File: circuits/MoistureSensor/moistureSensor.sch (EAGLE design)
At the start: 2 parts, among them Q1 BSS84

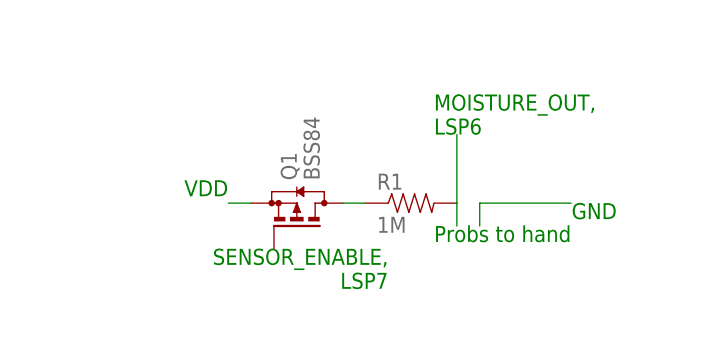
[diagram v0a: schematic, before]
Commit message: Added Moisture Sensor layout
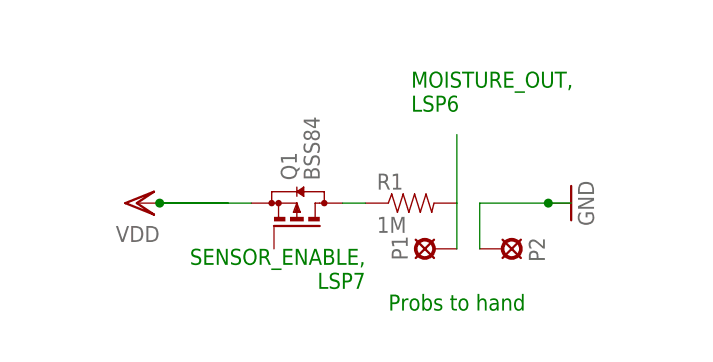
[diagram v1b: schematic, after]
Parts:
- added P1, P2: MCS10B, solpad:MCS10B
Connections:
- net N$2 renamed VDD
- new net GND: P2.MP
- net N$3: now also P1.MP
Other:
- note removed: "GND"
- note removed: "VDD"
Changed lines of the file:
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@@
 <part name="R1" library="SparkFun-Resistors" deviceset="1MOHM-1/10W-1%(0603)" device="" value="1M"/>
 <part name="Q1" library="transistor-small-signal" deviceset="BSS84" device=""/>
+<part name="GND1" library="supply1" deviceset="GND" device=""/>
+<part name="VDD1" library="supply1" deviceset="VDD" device=""/>
+<part name="P1" library="solpad" deviceset="MCS10B" device=""/>
+<part name="P2" library="solpad" deviceset="MCS10B" device=""/>
 </parts>
 <sheets>
 <sheet>
 <plain>
-<text x="12.7" y="66.04" size="1.778" layer="91">MOISTURE_OUT,
+<text x="10.16" y="68.58" size="1.778" layer="91">MOISTURE_OUT,
 LSP6</text>
-<text x="7.62" y="53.34" size="1.778" layer="91" rot="R180">SENSOR_ENABLE,
+<text x="5.08" y="53.34" size="1.778" layer="91" rot="R180">SENSOR_ENABLE,
 LSP7</text>
-<text x="-10.16" y="60.96" size="1.778" layer="91" rot="R180">VDD</text>
-<text x="33.02" y="58.42" size="1.778" layer="91" rot="R180">GND</text>
-<text x="27.94" y="55.88" size="1.778" layer="91" rot="R180">Probs to hand</text>
+<text x="22.86" y="48.26" size="1.778" layer="91" rot="R180">Probs to hand</text>
 </plain>
 <instances>
 <instance part="R1" gate="G$1" x="10.16" y="58.42"/>
 <instance part="Q1" gate="G$1" x="-2.54" y="58.42" rot="R90"/>
+<instance part="GND1" gate="1" x="27.94" y="58.42" rot="R90"/>
+<instance part="VDD1" gate="G$1" x="-20.32" y="58.42" rot="R90"/>
+<instance part="P1" gate="1" x="12.7" y="53.34" rot="R90"/>
+<instance part="P2" gate="1" x="20.32" y="53.34" rot="R270"/>
 </instances>
 <busses>
@@
 </segment>
 </net>
-<net name="N$2" class="0">
-<segment>
-<pinref part="Q1" gate="G$1" pin="S"/>
-<wire x1="-7.62" y1="58.42" x2="-10.16" y2="58.42" width="0.1524" layer="91"/>
-</segment>
-</net>
 <net name="N$3" class="0">
 <segment>
 <pinref part="R1" gate="G$1" pin="2"/>
-<wire x1="15.24" y1="58.42" x2="15.24" y2="55.88" width="0.1524" layer="91"/>
 <wire x1="15.24" y1="58.42" x2="15.24" y2="66.04" width="0.1524" layer="91"/>
+<pinref part="P1" gate="1" pin="MP"/>
+<wire x1="15.24" y1="58.42" x2="15.24" y2="53.34" width="0.1524" layer="91"/>
 </segment>
 </net>
-<net name="N$4" class="0">
+<net name="GND" class="0">
 <segment>
-<wire x1="17.78" y1="55.88" x2="17.78" y2="58.42" width="0.1524" layer="91"/>
-<wire x1="17.78" y1="58.42" x2="27.94" y2="58.42" width="0.1524" layer="91"/>
+<wire x1="17.78" y1="58.42" x2="25.4" y2="58.42" width="0.1524" layer="91"/>
+<pinref part="GND1" gate="1" pin="GND"/>
+<wire x1="25.4" y1="58.42" x2="27.94" y2="58.42" width="0.1524" layer="91"/>
+<junction x="25.4" y="58.42"/>
+<pinref part="P2" gate="1" pin="MP"/>
+<wire x1="17.78" y1="58.42" x2="17.78" y2="53.34" width="0.1524" layer="91"/>
 </segment>
 </net>
+<net name="VDD" class="0">
+<segment>
+<pinref part="Q1" gate="G$1" pin="S"/>
+<wire x1="-17.78" y1="58.42" x2="-10.16" y2="58.42" width="0.1524" layer="91"/>
+<pinref part="VDD1" gate="G$1" pin="VDD"/>
+<junction x="-17.78" y="58.42"/>
+<wire x1="-17.78" y1="58.42" x2="-7.62" y2="58.42" width="0.1524" layer="91"/>
+</segment>
+</net>

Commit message: Moisture sesnsor layout final
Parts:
- added EN, GND, OUT, VDD: MCS10B, solpad:MCS10B
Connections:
- new net N$2: EN.MP, Q1.G
- net GND: now also GND.MP
- net N$3: now also OUT.MP
- net VDD: now also VDD.MP
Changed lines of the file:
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@@
 <grid distance="0.1" unitdist="inch" unit="inch" style="lines" multiple="1" display="no" altdistance="0.01" altunitdist="inch" altunit="inch"/>
 <layers>
-<layer number="1" name="Top" color="4" fill="1" visible="no" active="no"/>
-<layer number="16" name="Bottom" color="1" fill="1" visible="no" active="no"/>
-<layer number="17" name="Pads" color="2" fill="1" visible="no" active="no"/>
-<layer number="18" name="Vias" color="2" fill="1" visible="no" active="no"/>
-<layer number="19" name="Unrouted" color="6" fill="1" visible="no" active="no"/>
-<layer number="20" name="Dimension" color="15" fill="1" visible="no" active="no"/>
-<layer number="21" name="tPlace" color="7" fill="1" visible="no" active="no"/>
-<layer number="22" name="bPlace" color="7" fill="1" visible="no" active="no"/>
-<layer number="23" name="tOrigins" color="15" fill="1" visible="no" active="no"/>
-<layer number="24" name="bOrigins" color="15" fill="1" visible="no" active="no"/>
-<layer number="25" name="tNames" color="7" fill="1" visible="no" active="no"/>
-<layer number="26" name="bNames" color="7" fill="1" visible="no" active="no"/>
-<layer number="27" name="tValues" color="7" fill="1" visible="no" active="no"/>
-<layer number="28" name="bValues" color="7" fill="1" visible="no" active="no"/>
+<layer number="1" name="Top" color="4" fill="1" visible="yes" active="no"/>
+<layer number="16" name="Bottom" color="1" fill="1" visible="yes" active="no"/>
+<layer number="17" name="Pads" color="2" fill="1" visible="yes" active="no"/>
+<layer number="18" name="Vias" color="2" fill="1" visible="yes" active="no"/>
+<layer number="19" name="Unrouted" color="6" fill="1" visible="yes" active="no"/>
+<layer number="20" name="Dimension" color="15" fill="1" visible="yes" active="no"/>
+<layer number="21" name="tPlace" color="7" fill="1" visible="yes" active="no"/>
+<layer number="22" name="bPlace" color="7" fill="1" visible="yes" active="no"/>
+<layer number="23" name="tOrigins" color="15" fill="1" visible="yes" active="no"/>
+<layer number="24" name="bOrigins" color="15" fill="1" visible="yes" active="no"/>
+<layer number="25" name="tNames" color="7" fill="1" visible="yes" active="no"/>
+<layer number="26" name="bNames" color="7" fill="1" visible="yes" active="no"/>
+<layer number="27" name="tValues" color="7" fill="1" visible="yes" active="no"/>
+<layer number="28" name="bValues" color="7" fill="1" visible="yes" active="no"/>
 <layer number="29" name="tStop" color="7" fill="3" visible="no" active="no"/>
 <layer number="30" name="bStop" color="7" fill="6" visible="no" active="no"/>
@@
 <layer number="35" name="tGlue" color="7" fill="4" visible="no" active="no"/>
 <layer number="36" name="bGlue" color="7" fill="5" visible="no" active="no"/>
-<layer number="37" name="tTest" color="7" fill="1" visible="no" active="no"/>
-<layer number="38" name="bTest" color="7" fill="1" visible="no" active="no"/>
+<layer number="37" name="tTest" color="7" fill="1" visible="yes" active="no"/>
+<layer number="38" name="bTest" color="7" fill="1" visible="yes" active="no"/>
 <layer number="39" name="tKeepout" color="4" fill="11" visible="no" active="no"/>
 <layer number="40" name="bKeepout" color="1" fill="11" visible="no" active="no"/>
@@
 <layer number="44" name="Drills" color="7" fill="1" visible="no" active="no"/>
 <layer number="45" name="Holes" color="7" fill="1" visible="no" active="no"/>
-<layer number="46" name="Milling" color="3" fill="1" visible="no" active="no"/>
-<layer number="47" name="Measures" color="7" fill="1" visible="no" active="no"/>
-<layer number="48" name="Document" color="7" fill="1" visible="no" active="no"/>
-<layer number="49" name="Reference" color="13" fill="1" visible="no" active="no"/>
-<layer number="50" name="dxf" color="7" fill="1" visible="no" active="no"/>
-<layer number="51" name="tDocu" color="14" fill="1" visible="no" active="no"/>
-<layer number="52" name="bDocu" color="7" fill="1" visible="no" active="no"/>
-<layer number="53" name="tGND_GNDA" color="7" fill="9" visible="no" active="no"/>
-<layer number="54" name="bGND_GNDA" color="1" fill="9" visible="no" active="no"/>
-<layer number="56" name="wert" color="7" fill="1" visible="no" active="no"/>
-<layer number="57" name="tCAD" color="7" fill="1" visible="no" active="no"/>
+<layer number="46" name="Milling" color="3" fill="1" visible="yes" active="no"/>
+<layer number="47" name="Measures" color="7" fill="1" visible="yes" active="no"/>
+<layer number="48" name="Document" color="7" fill="1" visible="yes" active="no"/>
+<layer number="49" name="Reference" color="7" fill="1" visible="yes" active="no"/>
+<layer number="50" name="dxf" color="7" fill="1" visible="yes" active="no"/>
+<layer number="51" name="tDocu" color="7" fill="1" visible="yes" active="no"/>
+<layer number="52" name="bDocu" color="7" fill="1" visible="yes" active="no"/>
+<layer number="53" name="tGND_GNDA" color="7" fill="9" visible="yes" active="no"/>
+<layer number="54" name="bGND_GNDA" color="1" fill="9" visible="yes" active="no"/>
+<layer number="56" name="wert" color="7" fill="1" visible="yes" active="no"/>
+<layer number="57" name="tCAD" color="7" fill="1" visible="yes" active="no"/>
 <layer number="90" name="Modules" color="5" fill="1" visible="yes" active="yes"/>
 <layer number="91" name="Nets" color="2" fill="1" visible="yes" active="yes"/>
@@
 <part name="P1" library="solpad" deviceset="MCS10B" device=""/>
 <part name="P2" library="solpad" deviceset="MCS10B" device=""/>
+<part name="GND" library="solpad" deviceset="MCS10B" device=""/>
+<part name="VDD" library="solpad" deviceset="MCS10B" device=""/>
+<part name="EN" library="solpad" deviceset="MCS10B" device=""/>
+<part name="OUT" library="solpad" deviceset="MCS10B" device=""/>
 </parts>
 <sheets>
@@
 <text x="10.16" y="68.58" size="1.778" layer="91">MOISTURE_OUT,
 LSP6</text>
-<text x="5.08" y="53.34" size="1.778" layer="91" rot="R180">SENSOR_ENABLE,
+<text x="2.54" y="48.26" size="1.778" layer="91" rot="R180">SENSOR_ENABLE,
 LSP7</text>
 <text x="22.86" y="48.26" size="1.778" layer="91" rot="R180">Probs to hand</text>
@@
 <instance part="P1" gate="1" x="12.7" y="53.34" rot="R90"/>
 <instance part="P2" gate="1" x="20.32" y="53.34" rot="R270"/>
+<instance part="GND" gate="1" x="25.4" y="60.96"/>
+<instance part="VDD" gate="1" x="-17.78" y="60.96"/>
+<instance part="EN" gate="1" x="-7.62" y="50.8" rot="R90"/>
+<instance part="OUT" gate="1" x="15.24" y="60.96"/>
 </instances>
 <busses>
@@
 <segment>
 <pinref part="R1" gate="G$1" pin="2"/>
-<wire x1="15.24" y1="58.42" x2="15.24" y2="66.04" width="0.1524" layer="91"/>
 <pinref part="P1" gate="1" pin="MP"/>
 <wire x1="15.24" y1="58.42" x2="15.24" y2="53.34" width="0.1524" layer="91"/>
+<pinref part="OUT" gate="1" pin="MP"/>
+<junction x="15.24" y="58.42"/>
 </segment>
 </net>
@@
 <pinref part="P2" gate="1" pin="MP"/>
 <wire x1="17.78" y1="58.42" x2="17.78" y2="53.34" width="0.1524" layer="91"/>
+<pinref part="GND" gate="1" pin="MP"/>
 </segment>
 </net>
@@
 <junction x="-17.78" y="58.42"/>
 <wire x1="-17.78" y1="58.42" x2="-7.62" y2="58.42" width="0.1524" layer="91"/>
-</segment>
-</net>
+<pinref part="VDD" gate="1" pin="MP"/>
+</segment>
+</net>
+<net name="N$2" class="0">
+<segment>
+<pinref part="EN" gate="1" pin="MP"/>
+<pinref part="Q1" gate="G$1" pin="G"/>
+<wire x1="-5.08" y1="50.8" x2="-5.08" y2="53.34" width="0.1524" layer="91"/>
+</segment>
+</net>
